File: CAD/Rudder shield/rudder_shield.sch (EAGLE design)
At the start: 8 parts

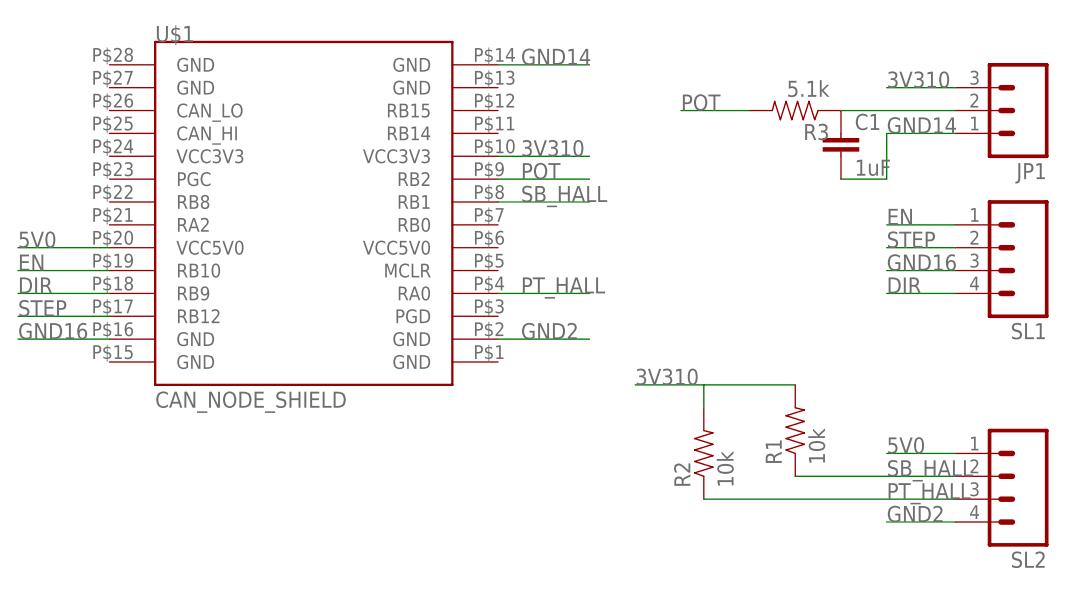
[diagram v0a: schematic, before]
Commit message: Updated the rudder shield to the new v3 CANode shield design.
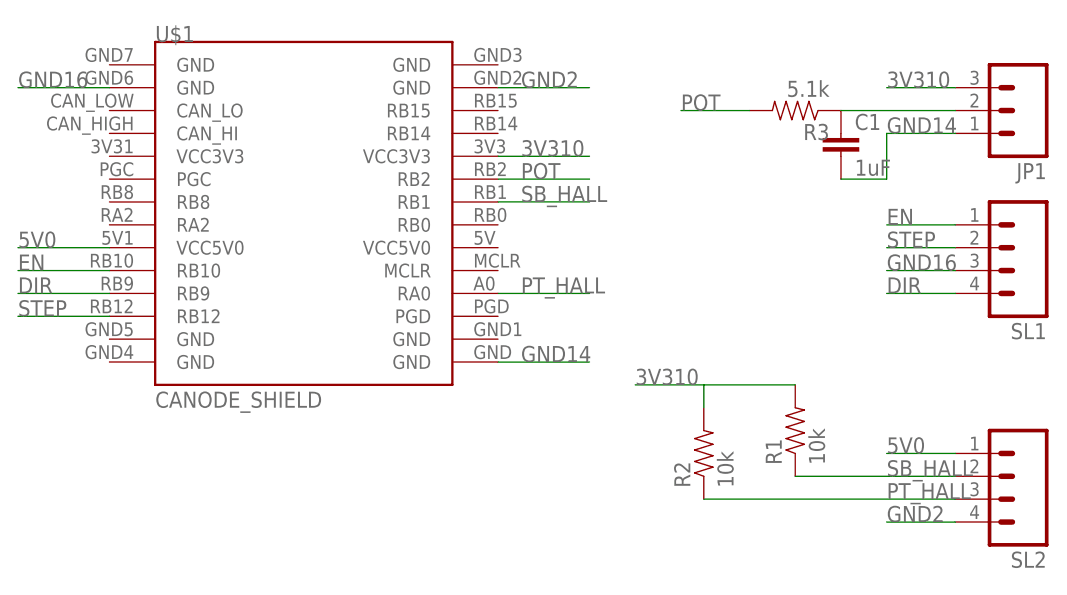
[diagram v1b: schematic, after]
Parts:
- U$1: value CAN_NODE_SHIELD -> CANODE_SHIELD; device ASL:CAN_NODE_SHIELD -> ASL:CANODE_SHIELD
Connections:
- net GND14: now also U$1.GND@1; no longer U$1.GND@14
- net GND16: now also U$1.GND@27; no longer U$1.GND@16
- net GND2: now also U$1.GND@13; no longer U$1.GND@2
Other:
- moved on the sheet: U$1
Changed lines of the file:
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@@
 <class number="0" name="default" width="0" drill="0">
+</class>
+<class number="1" name="small" width="0.2032" drill="0">
 </class>
 </classes>
 <parts>
-<part name="U$1" library="ASL" deviceset="CAN_NODE_SHIELD" device=""/>
+<part name="U$1" library="ASL" deviceset="CANODE_SHIELD" device=""/>
 <part name="JP1" library="ASL" deviceset="M03" device="LOCK"/>
 <part name="SL1" library="ASL" deviceset="M04" device="LOCK"/>
@@
 <net name="GND14" class="0">
 <segment>
-<wire x1="78.74" y1="43.18" x2="88.9" y2="43.18" width="0.1524" layer="91"/>
-<label x="81.28" y="43.18" size="1.778" layer="95"/>
-<pinref part="U$1" gate="G$1" pin="GND@14"/>
-</segment>
-<segment>
 <wire x1="129.54" y1="35.56" x2="121.92" y2="35.56" width="0.1524" layer="91"/>
 <wire x1="121.92" y1="35.56" x2="121.92" y2="30.48" width="0.1524" layer="91"/>
@@
 <pinref part="JP1" gate="G$1" pin="1"/>
 <pinref part="C1" gate="G$1" pin="2"/>
+</segment>
+<segment>
+<pinref part="U$1" gate="G$1" pin="GND@1"/>
+<wire x1="78.74" y1="10.16" x2="88.9" y2="10.16" width="0.1524" layer="91"/>
+<label x="81.28" y="10.16" size="1.778" layer="95"/>
 </segment>
 </net>
@@
 </segment>
 </net>
-<net name="EN" class="0">
+<net name="EN" class="1">
 <segment>
 <wire x1="129.54" y1="25.4" x2="121.92" y2="25.4" width="0.1524" layer="91"/>
@@
 </segment>
 </net>
-<net name="DIR" class="0">
+<net name="DIR" class="1">
 <segment>
 <wire x1="121.92" y1="17.78" x2="129.54" y2="17.78" width="0.1524" layer="91"/>
@@
 </segment>
 </net>
-<net name="STEP" class="0">
+<net name="STEP" class="1">
 <segment>
 <wire x1="121.92" y1="22.86" x2="129.54" y2="22.86" width="0.1524" layer="91"/>
@@
 </segment>
 </net>
-<net name="GND16" class="0">
-<segment>
-<wire x1="35.56" y1="12.7" x2="25.4" y2="12.7" width="0.1524" layer="91"/>
-<label x="25.4" y="12.7" size="1.778" layer="95"/>
-<pinref part="U$1" gate="G$1" pin="GND@16"/>
-</segment>
+<net name="GND16" class="1">
 <segment>
 <wire x1="129.54" y1="20.32" x2="121.92" y2="20.32" width="0.1524" layer="91"/>
@@
 <pinref part="SL1" gate="G$1" pin="3"/>
 </segment>
+<segment>
+<pinref part="U$1" gate="G$1" pin="GND@27"/>
+<wire x1="35.56" y1="40.64" x2="25.4" y2="40.64" width="0.1524" layer="91"/>
+<label x="25.4" y="40.64" size="1.778" layer="95"/>
+</segment>
 </net>
 <net name="GND2" class="0">
-<segment>
-<wire x1="78.74" y1="12.7" x2="88.9" y2="12.7" width="0.1524" layer="91"/>
-<label x="81.28" y="12.7" size="1.778" layer="95"/>
-<pinref part="U$1" gate="G$1" pin="GND@2"/>
-</segment>
 <segment>
 <wire x1="121.92" y1="-7.62" x2="129.54" y2="-7.62" width="0.1524" layer="91"/>
@@
 <pinref part="SL2" gate="G$1" pin="4"/>
 </segment>
+<segment>
+<pinref part="U$1" gate="G$1" pin="GND@13"/>
+<wire x1="78.74" y1="40.64" x2="88.9" y2="40.64" width="0.1524" layer="91"/>
+<label x="81.28" y="40.64" size="1.778" layer="95"/>
+</segment>
 </net>

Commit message: Updated all CANode shields to fit the latest version of it.
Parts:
- JP1: value (none) -> M03LOCK
